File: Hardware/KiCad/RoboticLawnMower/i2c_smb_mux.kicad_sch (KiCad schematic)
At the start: 7 parts, among them J6 Conn_01x04, J7 Conn_01x04, J8 Conn_01x04, J9 Conn_01x04, U14 PCA9547BS

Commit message: layout update
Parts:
- added J13: Conn_01x04, Connector_JST:JST_XA_B04B-XASK-1-A_1x04_P2.50mm_Vertical, symbol Connector_Generic:Conn_01x04
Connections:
- net +3.3V: now also J13.1 (Pin_1)
- net GND: now also J13.4 (Pin_4)
- net SCL: now also J13.2 (Pin_2)
- net SDA: now also J13.3 (Pin_3)
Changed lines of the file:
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@@
   (junction (at 203.2 52.07) (diameter 0) (color 0 0 0 0)
   )
+  (junction (at 203.2 29.21) (diameter 0) (color 0 0 0 0)
+  )
   (junction (at 207.01 85.09) (diameter 0) (color 0 0 0 0)
   )
   (junction (at 203.2 77.47) (diameter 0) (color 0 0 0 0)
   )
+  (junction (at 106.68 72.39) (diameter 0) (color 0 0 0 0)
+  )
   (junction (at 207.01 97.79) (diameter 0) (color 0 0 0 0)
   )
+  (junction (at 207.01 59.69) (diameter 0) (color 0 0 0 0)
+  )
   (junction (at 203.2 64.77) (diameter 0) (color 0 0 0 0)
   )
+  (junction (at 104.14 69.85) (diameter 0) (color 0 0 0 0)
+  )
   (junction (at 207.01 72.39) (diameter 0) (color 0 0 0 0)
   )
@@
     (stroke (width 0) (type default) (color 0 0 0 0))
   )
+  (wire (pts (xy 106.68 72.39) (xy 134.62 72.39))
+    (stroke (width 0) (type default) (color 0 0 0 0))
+  )
+  (wire (pts (xy 209.55 34.29) (xy 106.68 34.29))
+    (stroke (width 0) (type default) (color 0 0 0 0))
+  )
+  (wire (pts (xy 203.2 29.21) (xy 203.2 52.07))
+    (stroke (width 0) (type default) (color 0 0 0 0))
+  )
   (wire (pts (xy 154.94 82.55) (xy 209.55 82.55))
     (stroke (width 0) (type default) (color 0 0 0 0))
@@
     (stroke (width 0) (type default) (color 0 0 0 0))
   )
+  (wire (pts (xy 203.2 29.21) (xy 209.55 29.21))
+    (stroke (width 0) (type default) (color 0 0 0 0))
+  )
   (wire (pts (xy 209.55 57.15) (xy 167.64 57.15))
     (stroke (width 0) (type default) (color 0 0 0 0))
@@
     (stroke (width 0) (type default) (color 0 0 0 0))
   )
+  (wire (pts (xy 106.68 34.29) (xy 106.68 72.39))
+    (stroke (width 0) (type default) (color 0 0 0 0))
+  )
   (wire (pts (xy 203.2 77.47) (xy 209.55 77.47))
     (stroke (width 0) (type default) (color 0 0 0 0))
@@
     (stroke (width 0) (type default) (color 0 0 0 0))
   )
-  (wire (pts (xy 88.9 72.39) (xy 134.62 72.39))
-    (stroke (width 0) (type default) (color 0 0 0 0))
-  )
-  (wire (pts (xy 203.2 48.26) (xy 203.2 52.07))
+  (wire (pts (xy 207.01 36.83) (xy 207.01 59.69))
+    (stroke (width 0) (type default) (color 0 0 0 0))
+  )
+  (wire (pts (xy 88.9 72.39) (xy 106.68 72.39))
+    (stroke (width 0) (type default) (color 0 0 0 0))
+  )
+  (wire (pts (xy 203.2 24.13) (xy 203.2 29.21))
     (stroke (width 0) (type default) (color 0 0 0 0))
   )
@@
     (stroke (width 0) (type default) (color 0 0 0 0))
   )
+  (wire (pts (xy 104.14 69.85) (xy 134.62 69.85))
+    (stroke (width 0) (type default) (color 0 0 0 0))
+  )
   (wire (pts (xy 207.01 72.39) (xy 209.55 72.39))
     (stroke (width 0) (type default) (color 0 0 0 0))
@@
     (stroke (width 0) (type default) (color 0 0 0 0))
   )
-  (wire (pts (xy 88.9 69.85) (xy 134.62 69.85))
+  (wire (pts (xy 88.9 69.85) (xy 104.14 69.85))
     (stroke (width 0) (type default) (color 0 0 0 0))
   )
@@
     (stroke (width 0) (type default) (color 0 0 0 0))
   )
+  (wire (pts (xy 209.55 31.75) (xy 104.14 31.75))
+    (stroke (width 0) (type default) (color 0 0 0 0))
+  )
+  (wire (pts (xy 104.14 31.75) (xy 104.14 69.85))
+    (stroke (width 0) (type default) (color 0 0 0 0))
+  )
   (wire (pts (xy 172.72 77.47) (xy 154.94 77.47))
     (stroke (width 0) (type default) (color 0 0 0 0))
@@
     (stroke (width 0) (type default) (color 0 0 0 0))
   )
+  (wire (pts (xy 209.55 36.83) (xy 207.01 36.83))
+    (stroke (width 0) (type default) (color 0 0 0 0))
+  )
   (wire (pts (xy 207.01 97.79) (xy 207.01 101.6))
     (stroke (width 0) (type default) (color 0 0 0 0))
@@
     (pin "2")
   )
-  (symbol (lib_id "power:+3.3V") (at 203.2 48.26 0) (unit 1)
-    (in_bom yes) (on_board yes) (fields_autoplaced)
-    (property "Reference" "#PWR039" (id 0) (at 203.2 52.07 0)
-      (effects (font (size 1.27 1.27)) hide)
-    )
-    (property "Value" "+3.3V" (id 1) (at 203.2 43.18 0))
-    (property "Footprint" "" (id 2) (at 203.2 48.26 0)
-      (effects (font (size 1.27 1.27)) hide)
-    )
-    (property "Datasheet" "" (id 3) (at 203.2 48.26 0)
+  (symbol (lib_id "power:+3.3V") (at 203.2 24.13 0) (unit 1)
+    (in_bom yes) (on_board yes) (fields_autoplaced)
+    (property "Reference" "#PWR039" (id 0) (at 203.2 27.94 0)
+      (effects (font (size 1.27 1.27)) hide)
+    )
+    (property "Value" "+3.3V" (id 1) (at 203.2 19.05 0))
+    (property "Footprint" "" (id 2) (at 203.2 24.13 0)
+      (effects (font (size 1.27 1.27)) hide)
+    )
+    (property "Datasheet" "" (id 3) (at 203.2 24.13 0)
       (effects (font (size 1.27 1.27)) hide)
     )
@@
       (effects (font (size 1.27 1.27)) hide)
     )
+    (pin "1")
+    (pin "2")
+    (pin "3")
+    (pin "4")
+  )
+  (symbol (lib_id "Connector_Generic:Conn_01x04") (at 214.63 31.75 0) (unit 1)
+    (in_bom yes) (on_board yes) (fields_autoplaced)
+    (property "Reference" "J13" (id 0) (at 217.17 31.7499 0)
+      (effects (font (size 1.27 1.27)) (justify left))
+    )
+    (property "Value" "Conn_01x04" (id 1) (at 217.17 34.2899 0)
+      (effects (font (size 1.27 1.27)) (justify left))
+    )
+    (property "Footprint" "Connector_JST:JST_XA_B04B-XASK-1-A_1x04_P2.50mm_Vertical" (id 2) (at 214.63 31.75 0)
+      (effects (font (size 1.27 1.27)) hide)
+    )
+    (property "Datasheet" "~" (id 3) (at 214.63 31.75 0)
+      (effects (font (size 1.27 1.27)) hide)
+    )

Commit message: Layout
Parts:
- added R19: 10K, Resistor_SMD:R_0603_1608Metric, symbol Device:R
- added R20, R21, R22, R23, R24, R25, R35, R36: 4k7, Resistor_SMD:R_0603_1608Metric, symbol Device:R
- added R37, R39: 10K, Resistor_SMD:R_0402_1005Metric, symbol Device:R
- added R38, R40: N.P., Resistor_SMD:R_0402_1005Metric, symbol Device:R
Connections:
- net ADR_2 is gone; now on net GND: U14.18 (A2)
- net +3.3V: now also R19.1, R20.2, R21.2, R22.2, R23.2, R24.2, R25.2, R35.2, R36.2, R37.1, R39.1
- net GND: now also R38.2, R40.2
- net ~{RESET}: now also R19.2
- net at J7.2 (Pin_2), U14.4 (SC1): now also R22.1
- net at J7.3 (Pin_3), U14.3 (SD1): now also R23.1
- net at J8.2 (Pin_2), U14.6 (SC2): now also R24.1
- net at J8.3 (Pin_3), U14.5 (SD2): now also R25.1
- net at J6.3 (Pin_3), U14.1 (SD0): now also R21.1
- net at J6.2 (Pin_2), U14.2 (SC0): now also R20.1
- net at J9.3 (Pin_3), U14.7 (SD3): now also R36.1
- net at J9.2 (Pin_2), U14.8 (SC3): now also R35.1
- net ADR_0: no longer names the net of U14.22 (A0)
- net ADR_0: now also R37.2, R38.1
- net ADR_1: no longer names the net of U14.23 (A1)
- net ADR_1: now also R39.2, R40.1

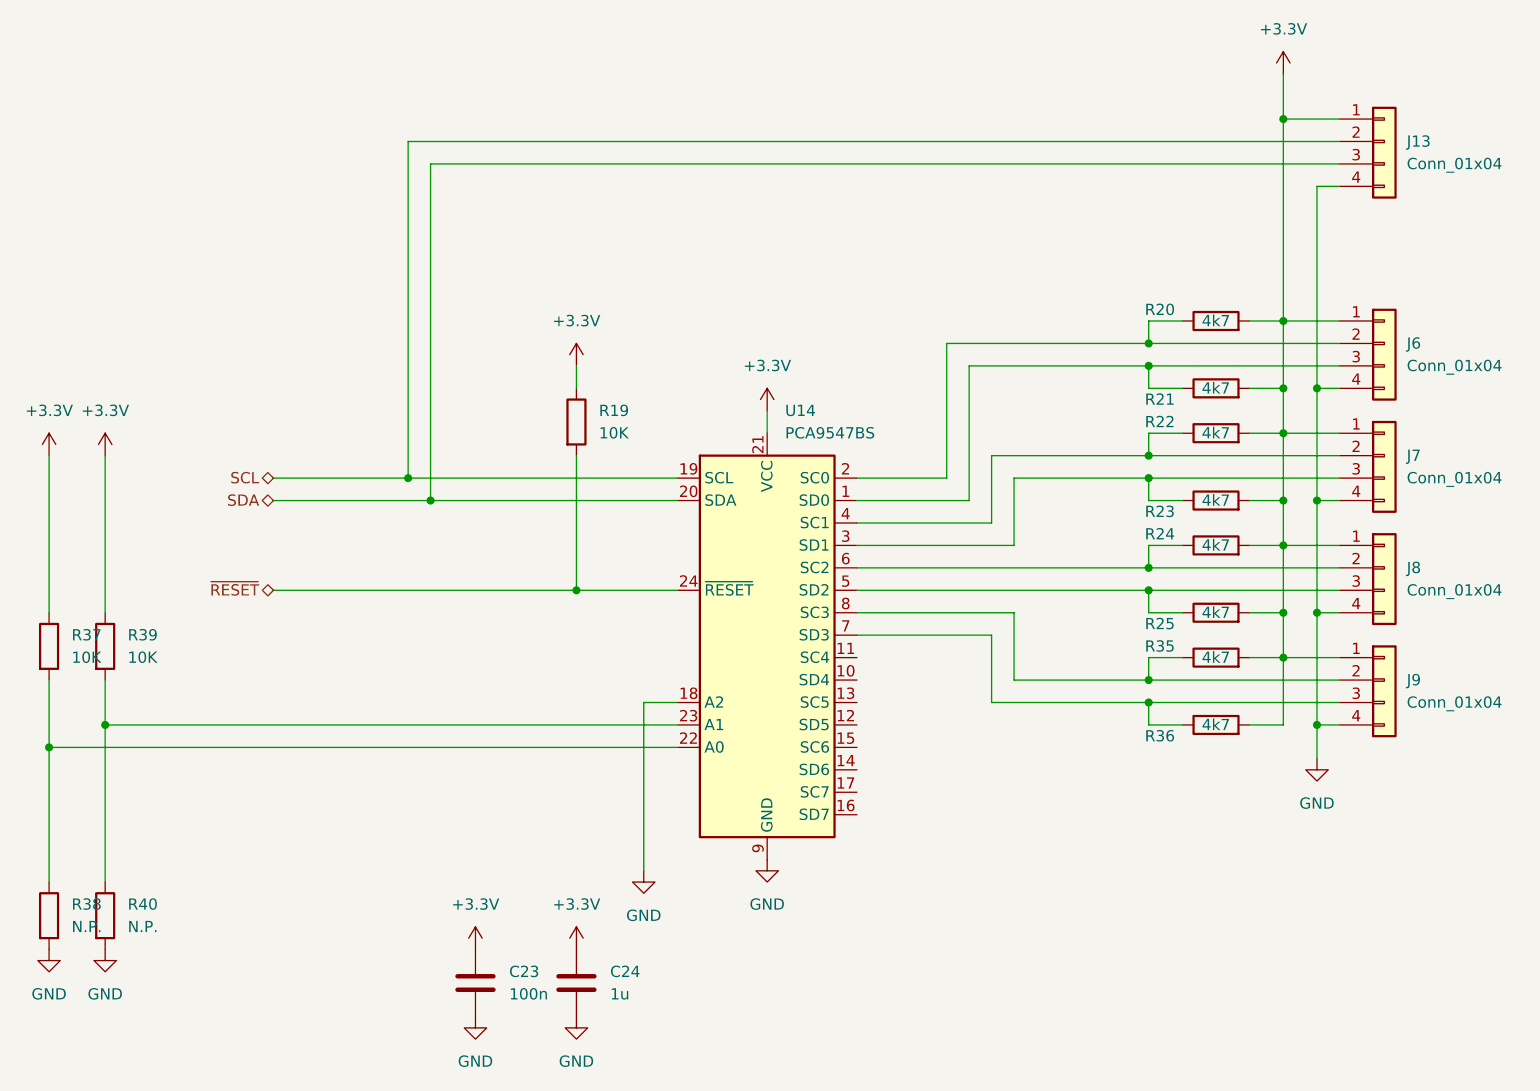
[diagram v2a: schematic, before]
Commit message: Schaltplan und Layout änderung
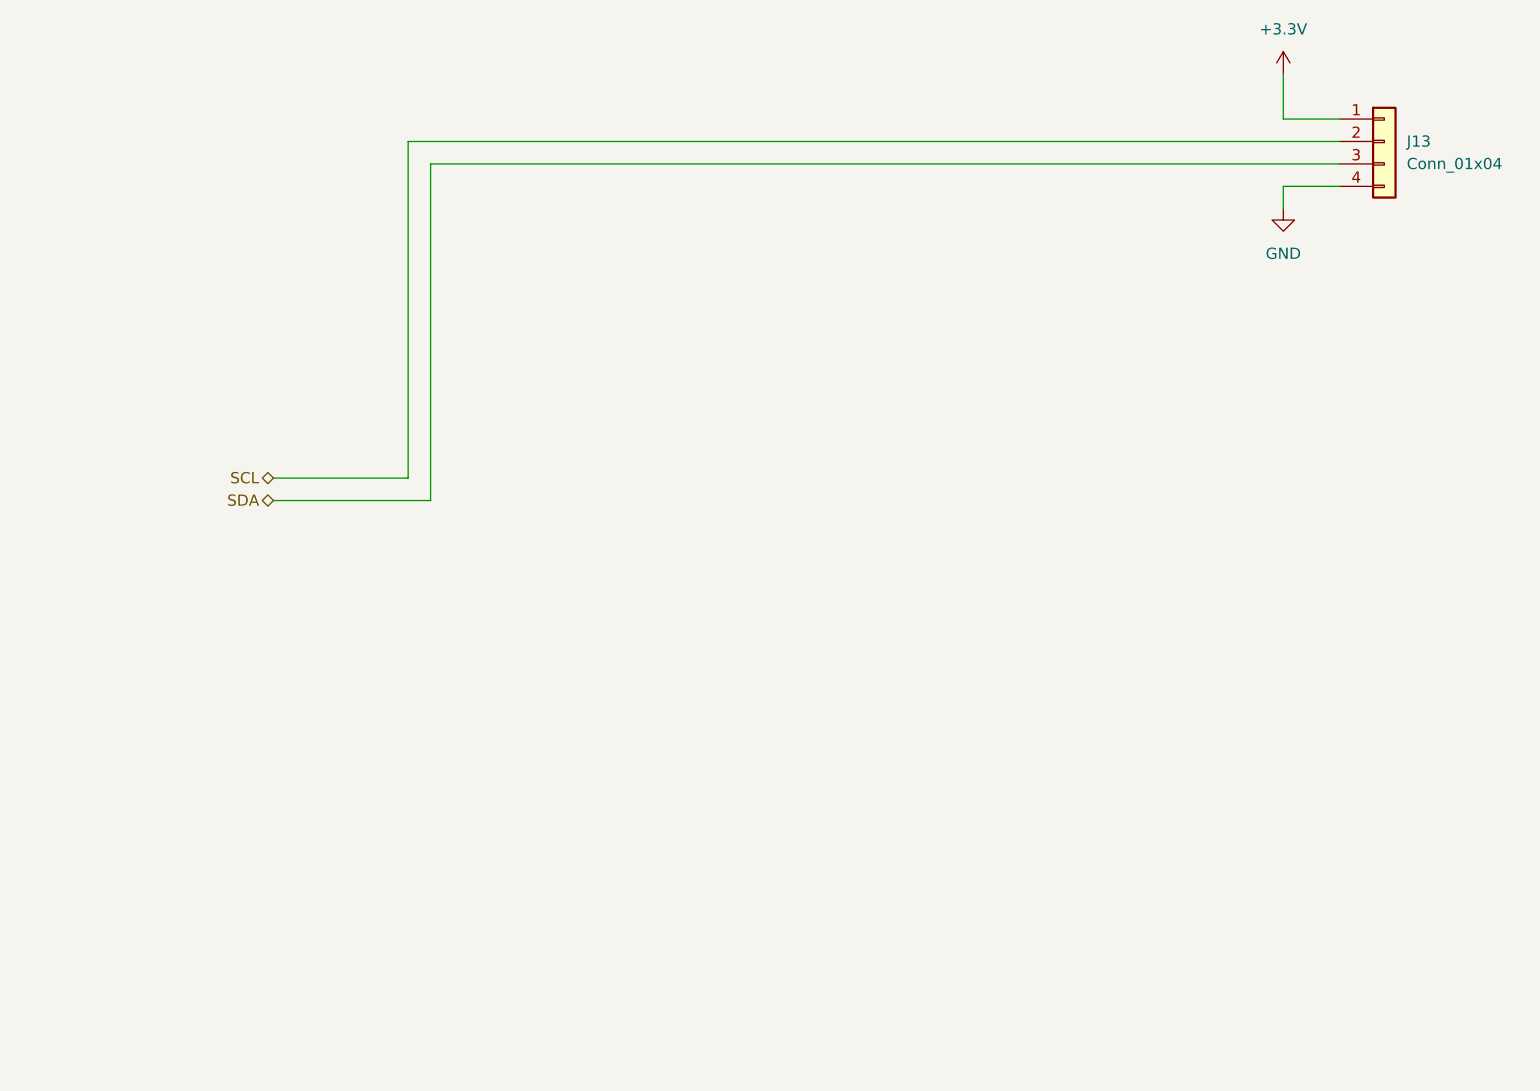
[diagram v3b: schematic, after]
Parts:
- removed C23: 100n, Capacitor_SMD:C_0603_1608Metric, symbol Device:C
- removed C24: 1u, Capacitor_SMD:C_0603_1608Metric, symbol Device:C
- removed J6, J7, J8, J9: Conn_01x04, Connector_JST:JST_XA_B04B-XASK-1-A_1x04_P2.50mm_Vertical, symbol Connector_Generic:Conn_01x04
- removed R19: 10K, Resistor_SMD:R_0603_1608Metric, symbol Device:R
- removed R20, R21, R22, R23, R24, R25, R35, R36: 4k7, Resistor_SMD:R_0603_1608Metric, symbol Device:R
- removed R37, R39: 10K, Resistor_SMD:R_0402_1005Metric, symbol Device:R
- removed R38, R40: N.P., Resistor_SMD:R_0402_1005Metric, symbol Device:R
- removed U14: PCA9547BS, Package_DFN_QFN:HVQFN-24-1EP_4x4mm_P0.5mm_EP2.1x2.1mm, symbol Interface_Expansion:PCA9547BS

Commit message: Layout
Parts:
- J13: footprint Connector_JST:JST_XA_B04B-XASK-1-A_1x04_P2.50mm_Vertical -> Connector_JST:JST_XA_B04B-XASK-1_1x04_P2.50mm_Vertical
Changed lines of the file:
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@@
       (effects (font (size 1.27 1.27)) (justify left))
     )
-    (property "Footprint" "Connector_JST:JST_XA_B04B-XASK-1-A_1x04_P2.50mm_Vertical" (id 2) (at 214.63 31.75 0)
+    (property "Footprint" "Connector_JST:JST_XA_B04B-XASK-1_1x04_P2.50mm_Vertical" (id 2) (at 214.63 31.75 0)
       (effects (font (size 1.27 1.27)) hide)
     )
